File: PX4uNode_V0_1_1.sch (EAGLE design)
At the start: 131 parts, among them M3_MOUNT1101 MOUNT-HOLE3.1MM, M3_MOUNT1102 MOUNT-HOLE3.1MM, M3_MOUNT1103 MOUNT-HOLE3.1MM, M3_MOUNT1104 MOUNT-HOLE3.1MM, U101 STM32F4X7VX, U401 MAX3051, U402 MAX3051, X101 3.2x2.5 mm / 24 MHz / 15 ppm

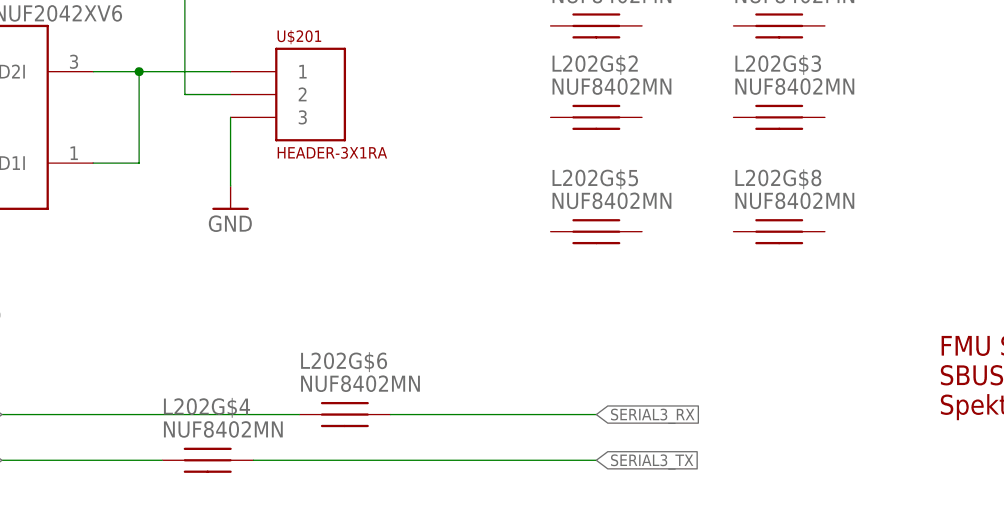
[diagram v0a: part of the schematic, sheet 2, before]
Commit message: uNode - Memory layout
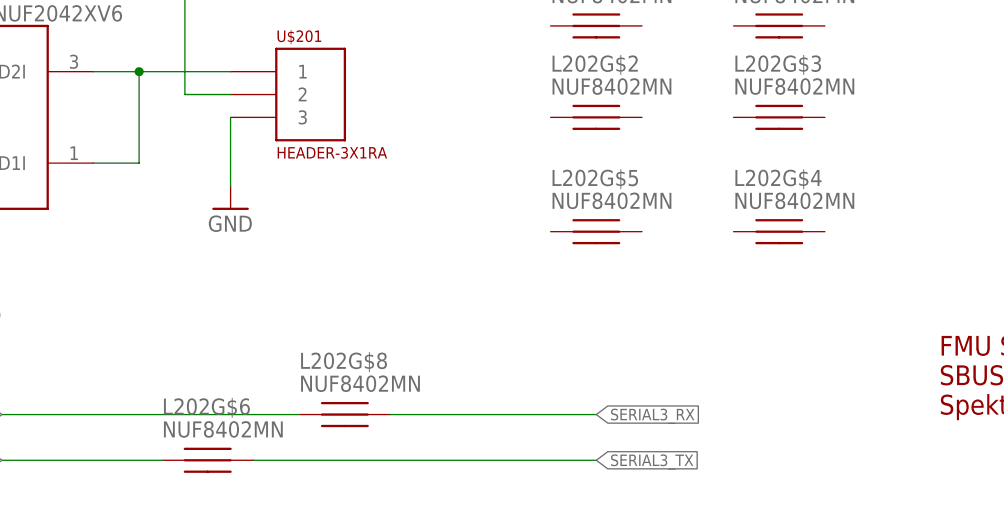
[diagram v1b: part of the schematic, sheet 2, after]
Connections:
- net FMU-UART7_RX: now also L202G$8.P$1; no longer L202G$6.P$1
- net FMU-UART7_TX: now also L202G$6.P$1; no longer L202G$4.P$1
- net SERIAL3_RX: now also L202G$8.P$2; no longer L202G$6.P$2
- net SERIAL3_TX: now also L202G$6.P$2; no longer L202G$4.P$2
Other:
- moved on the sheet: L202G$4, L202G$6, L202G$8
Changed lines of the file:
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@@
 <instance part="GND8" gate="1" x="144.78" y="134.62"/>
 <instance part="L202" gate="G$9" x="20.32" y="20.32"/>
-<instance part="L202" gate="G$6" x="99.06" y="17.78"/>
-<instance part="L202" gate="G$4" x="83.82" y="12.7"/>
+<instance part="L202" gate="G$8" x="99.06" y="17.78"/>
+<instance part="L202" gate="G$6" x="83.82" y="12.7"/>
 <instance part="L202" gate="G$1" x="127" y="60.96"/>
 <instance part="L202" gate="G$2" x="127" y="50.8"/>
@@
 <instance part="L202" gate="G$5" x="127" y="38.1"/>
 <instance part="L202" gate="G$7" x="147.32" y="60.96"/>
-<instance part="L202" gate="G$8" x="147.32" y="38.1"/>
+<instance part="L202" gate="G$4" x="147.32" y="38.1"/>
 <instance part="U$202" gate="G$1" x="83.82" y="99.06">
 <attribute name="PARTNO" x="83.82" y="99.06" size="1.778" layer="96" display="off"/>
@@
 <segment>
 <label x="127" y="12.7" size="1.27" layer="95" xref="yes"/>
-<pinref part="L202" gate="G$4" pin="P$2"/>
+<pinref part="L202" gate="G$6" pin="P$2"/>
 <wire x1="127" y1="12.7" x2="88.9" y2="12.7" width="0.1524" layer="91"/>
 </segment>
@@
 <segment>
 <label x="127" y="17.78" size="1.27" layer="95" xref="yes"/>
-<pinref part="L202" gate="G$6" pin="P$2"/>
+<pinref part="L202" gate="G$8" pin="P$2"/>
 <wire x1="127" y1="17.78" x2="104.14" y2="17.78" width="0.1524" layer="91"/>
 </segment>
@@
 <segment>
 <label x="60.96" y="17.78" size="1.27" layer="95" rot="R180" xref="yes"/>
+<pinref part="L202" gate="G$8" pin="P$1"/>
+<wire x1="60.96" y1="17.78" x2="93.98" y2="17.78" width="0.1524" layer="91"/>
+</segment>
+</net>
+<net name="FMU-UART7_TX" class="0">
+<segment>
+<label x="60.96" y="12.7" size="1.27" layer="95" rot="R180" xref="yes"/>
 <pinref part="L202" gate="G$6" pin="P$1"/>
-<wire x1="60.96" y1="17.78" x2="93.98" y2="17.78" width="0.1524" layer="91"/>
-</segment>
-</net>
-<net name="FMU-UART7_TX" class="0">
-<segment>
-<label x="60.96" y="12.7" size="1.27" layer="95" rot="R180" xref="yes"/>
-<pinref part="L202" gate="G$4" pin="P$1"/>
 <wire x1="78.74" y1="12.7" x2="60.96" y2="12.7" width="0.1524" layer="91"/>
 </segment>

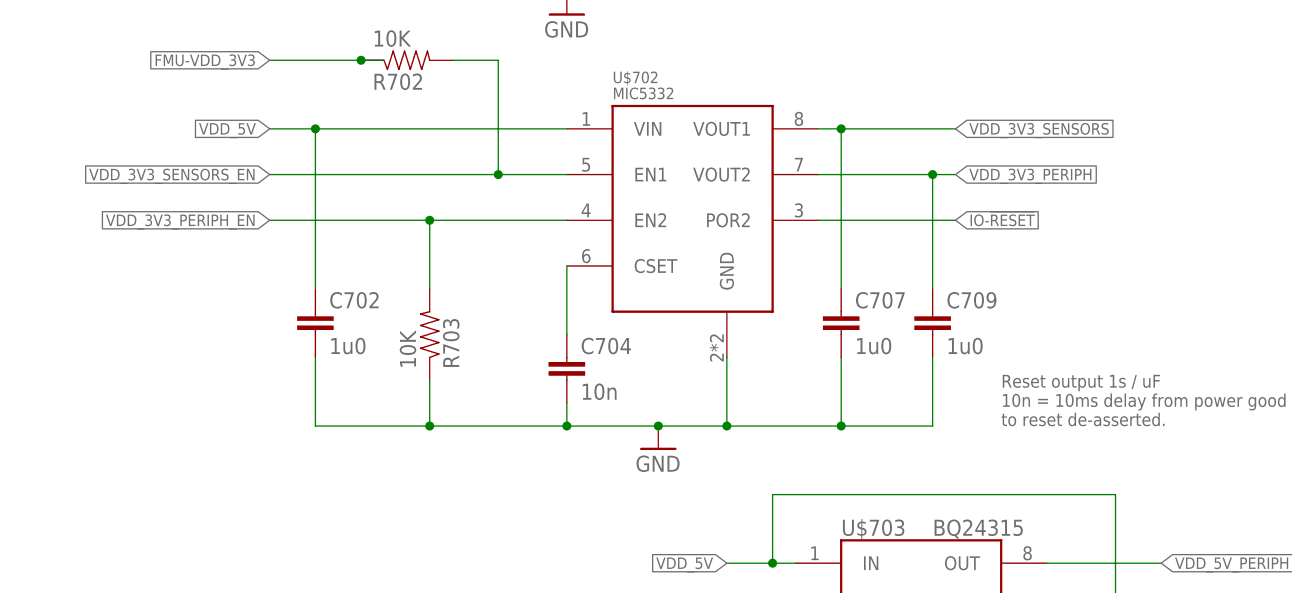
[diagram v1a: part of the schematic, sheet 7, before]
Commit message: Removed unused 3V3 peripheral power from regulator
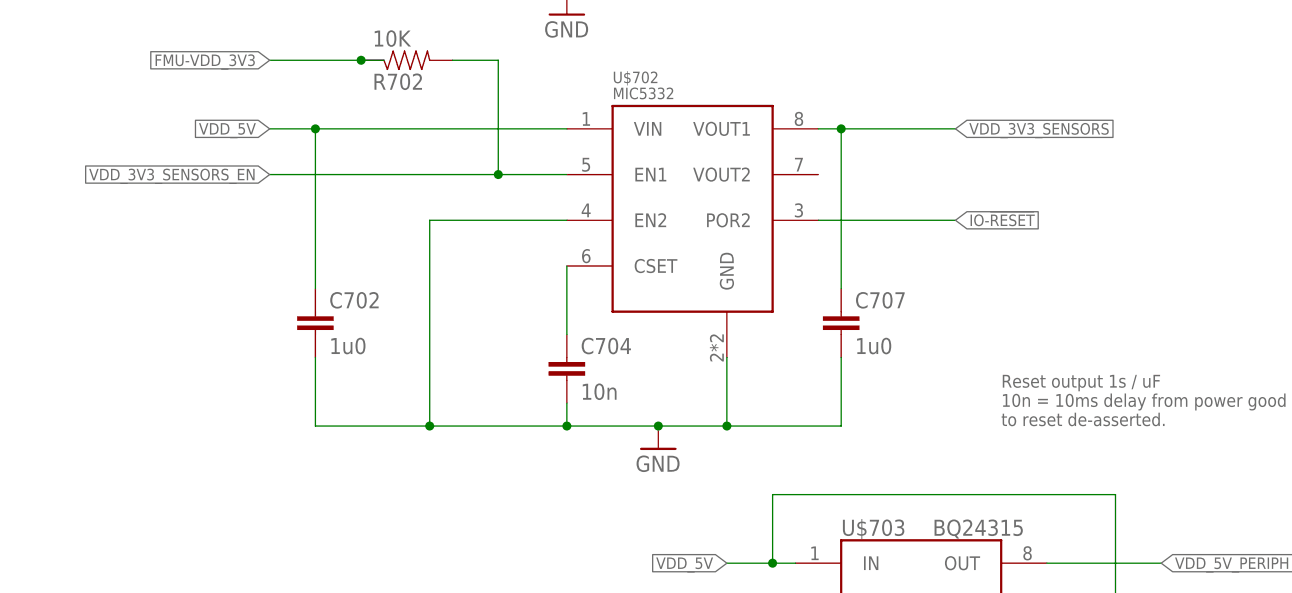
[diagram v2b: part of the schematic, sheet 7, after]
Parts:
- removed C709: 1u0, pixhawk2:CAP0603
- removed R703: 10K, pixhawk2:RESISTOR0402-RES
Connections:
- removed net VDD_3V3_PERIPH: C709.1, U$702.VOUT2
- removed net VDD_3V3_PERIPH_EN: R703.2, U$702.EN2
- net GND: now also U$702.EN2; no longer C709.2, R703.1
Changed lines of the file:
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@@
-<attribute name="PARTNO" value="CC0603ZRY5V7BB105"/>
-</part>
-<part name="C709" library="pixhawk2" deviceset="CAP" device="0603" value="1u0">
 <attribute name="PARTNO" value="CC0603ZRY5V7BB105"/>
 </part>
@@
 </part>
 <part name="R702" library="pixhawk2" deviceset="RESISTOR" device="0402-RES" value="10K">
-<attribute name="PARTNO" value="RC0402FR-0710KL"/>
-</part>
-<part name="R703" library="pixhawk2" deviceset="RESISTOR" device="0402-RES" value="10K">
 <attribute name="PARTNO" value="RC0402FR-0710KL"/>
 </part>
@@
 <attribute name="PARTNO" x="99.06" y="86.36" size="1.778" layer="96" display="off"/>
 </instance>
-<instance part="C709" gate="G$1" x="109.22" y="86.36">
-<attribute name="PARTNO" x="109.22" y="86.36" size="1.778" layer="96" display="off"/>
-</instance>
 <instance part="GND68" gate="1" x="78.74" y="73.66"/>
 <instance part="U$702" gate="G$1" x="81.28" y="104.14">
@@
 <attribute name="NAME" x="46.99" y="115.3414" size="1.778" layer="95" rot="MR180"/>
 <attribute name="VALUE" x="46.99" y="120.142" size="1.778" layer="96" rot="MR180"/>
-</instance>
-<instance part="R703" gate="G$1" x="53.34" y="86.36" smashed="yes" rot="MR90">
-<attribute name="PARTNO" x="53.34" y="86.36" size="1.778" layer="96" rot="MR90" display="off"/>
-<attribute name="NAME" x="54.8386" y="82.55" size="1.778" layer="95" rot="MR90"/>
-<attribute name="VALUE" x="50.038" y="82.55" size="1.778" layer="96" rot="MR90"/>
 </instance>
 <instance part="R701" gate="G$1" x="40.64" y="132.08" rot="R90">
@@
 <pinref part="GND68" gate="1" pin="GND"/>
 <junction x="78.74" y="76.2"/>
-<pinref part="C709" gate="G$1" pin="2"/>
 <wire x1="86.36" y1="76.2" x2="99.06" y2="76.2" width="0.1524" layer="91"/>
-<wire x1="99.06" y1="76.2" x2="109.22" y2="76.2" width="0.1524" layer="91"/>
-<wire x1="109.22" y1="76.2" x2="109.22" y2="83.82" width="0.1524" layer="91"/>
 <pinref part="C707" gate="G$1" pin="2"/>
 <wire x1="99.06" y1="83.82" x2="99.06" y2="76.2" width="0.1524" layer="91"/>
 <junction x="86.36" y="76.2"/>
-<junction x="99.06" y="76.2"/>
 <pinref part="C702" gate="G$1" pin="2"/>
 <wire x1="40.64" y1="83.82" x2="40.64" y2="76.2" width="0.1524" layer="91"/>
-<wire x1="40.64" y1="76.2" x2="53.34" y2="76.2" width="0.1524" layer="91"/>
 <junction x="68.58" y="76.2"/>
 <pinref part="U$702" gate="G$1" pin="GND"/>
+<wire x1="40.64" y1="76.2" x2="53.34" y2="76.2" width="0.1524" layer="91"/>
+<pinref part="U$702" gate="G$1" pin="EN2"/>
 <wire x1="53.34" y1="76.2" x2="68.58" y2="76.2" width="0.1524" layer="91"/>
-<pinref part="R703" gate="G$1" pin="1"/>
-<wire x1="53.34" y1="81.28" x2="53.34" y2="76.2" width="0.1524" layer="91"/>
+<wire x1="53.34" y1="99.06" x2="68.58" y2="99.06" width="0.1524" layer="91"/>
+<wire x1="53.34" y1="99.06" x2="53.34" y2="76.2" width="0.1524" layer="91"/>
 <junction x="53.34" y="76.2"/>
 </segment>
@@
 </segment>
 </net>
-<net name="VDD_3V3_PERIPH_EN" class="1">
-<segment>
-<label x="35.56" y="99.06" size="1.27" layer="95" rot="R180" xref="yes"/>
-<pinref part="U$702" gate="G$1" pin="EN2"/>
-<wire x1="35.56" y1="99.06" x2="53.34" y2="99.06" width="0.1524" layer="91"/>
-<pinref part="R703" gate="G$1" pin="2"/>
-<wire x1="53.34" y1="99.06" x2="68.58" y2="99.06" width="0.1524" layer="91"/>
-<wire x1="53.34" y1="91.44" x2="53.34" y2="99.06" width="0.1524" layer="91"/>
-<junction x="53.34" y="99.06"/>
-</segment>
-</net>
 <net name="VDD_3V3_SENSORS" class="1">
 <segment>
@@
 </segment>
 </net>
-<net name="VDD_3V3_PERIPH" class="1">
-<segment>
-<label x="111.76" y="104.14" size="1.27" layer="95" xref="yes"/>
-<wire x1="109.22" y1="104.14" x2="111.76" y2="104.14" width="0.1524" layer="91"/>
-<pinref part="C709" gate="G$1" pin="1"/>
-<wire x1="109.22" y1="91.44" x2="109.22" y2="104.14" width="0.1524" layer="91"/>
-<pinref part="U$702" gate="G$1" pin="VOUT2"/>
-<wire x1="109.22" y1="104.14" x2="96.52" y2="104.14" width="0.1524" layer="91"/>
-<junction x="109.22" y="104.14"/>
-</segment>
-</net>
